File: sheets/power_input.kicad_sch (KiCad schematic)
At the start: 106 parts, among them J2 TYPE-C-31-M-12, Q20 FDMS86250, Q21 FDMC2523P, Q22 BSC057N08NS3 G, Q23 BSC057N08NS3 G, Q24 FCX493TA, Q25 FCX493TA, Q30 IRLR7843TRPBF, Q31 IRLR7843TRPBF, T1 750313355, U10 TPS23730RMTR, U19 LM5050MKX-1/NOPB, U2 CH224K, U20 TCMT1107, U21 LM5050MKX-1/NOPB, U22 TL431IDBVR, U23 FOD817DS

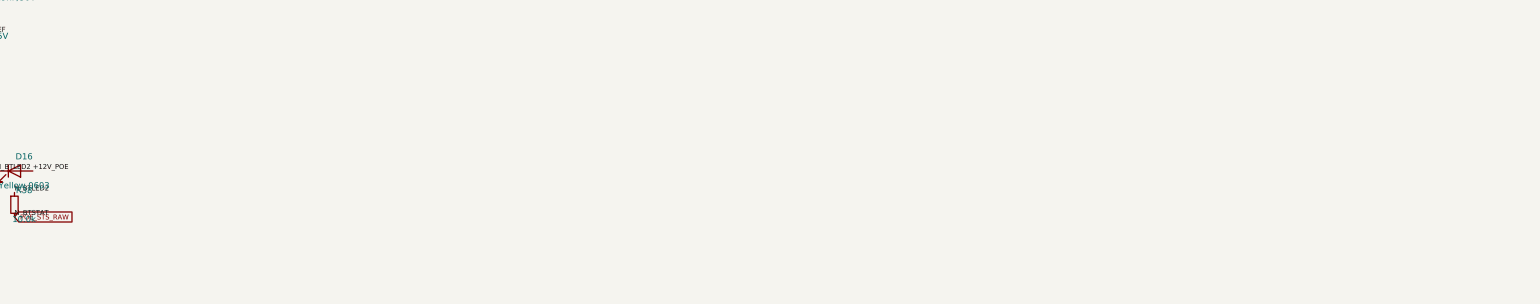
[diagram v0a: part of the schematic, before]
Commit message: sch: mcu fixes — XOUT crystal resistor, rail-to-rail LED kill, RGB series R, decoupling
Review pass on sheets/mcu.kicad_sch: swap R76 onto the XOUT side of Y1
(XIN direct, 1k limits drive into the crystal per the RPi RP2040 guide);
rebuild the LED-kill gate network rail-to-rail (Q35 2N7002 + repurposed
R82/R84 pull-ups replace the old resistive-mixing divider that left only
~0.2-0.3V of OFF-state Vgs margin — GP9/LED_EN_CTL is now active-low
kill); insert R92 (330R) between GP14 and U28 DIN with a net split
(RGB_DI/RGB_DIN); add decoupling (C78-C81 100nF at U25/U26/U27/RP2040's
9th supply pin, C82 1uF at VREG_VIN); add a Task-14 SW2 silk note and a
power_input.kicad_sch note on D16's unkillable ~75uA glow.

uv run tools/check_nets.py: all pass (new + all pre-existing lines).
kicad-cli sch erc: 0 errors / 611 warnings (600 baseline +11, all
endpoint_off_grid, no new category — see docs/erc-waivers.md).
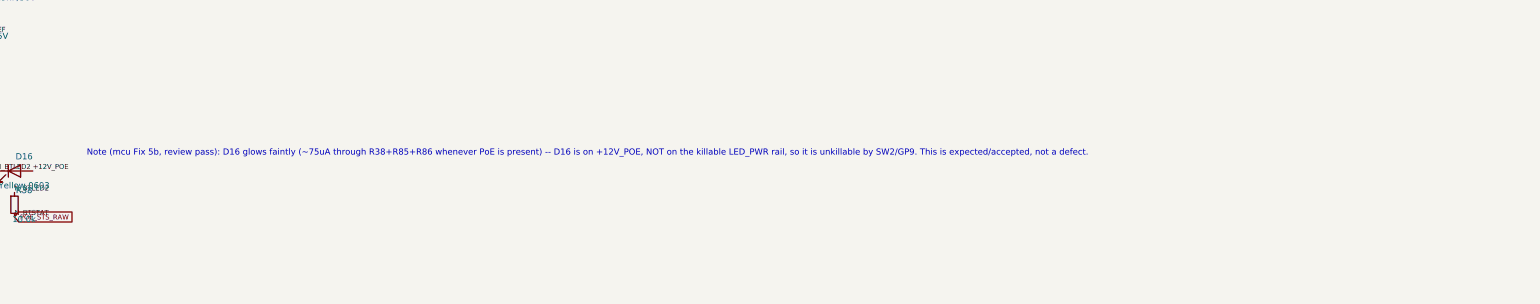
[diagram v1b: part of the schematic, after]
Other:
- note added: "Note (mcu Fix 5b, review pass): D16 glows faintly (~75uA through R38+R85+R86 whenever PoE is present) -- D16 is on +12V_POE, NOT on the killable LED_PWR rail, so it is unkillable by SW2/GP9. This is expected/accepted, not a defect."
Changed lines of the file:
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@@
 		)
+	)
+	(text "Note (mcu Fix 5b, review pass): D16 glows faintly (~75uA through R38+R85+R86 whenever PoE is present) -- D16 is on +12V_POE, NOT on the killable LED_PWR rail, so it is unkillable by SW2/GP9. This is expected/accepted, not a defect."
+		(exclude_from_sim no)
+		(at 555 140 0)
+		(effects (font (size 1.27 1.27)) (justify left bottom))
 	)
 	(text "TODO(mcu): POE_STATUS net dropped on this sheet — EVM-093 exposes BT only as an isolated LED indicator (U23 opto, D16/R38 from +12V_POE). Node N_BTSTAT swings ~0-11V, NOT 3V3-safe. Re-plan the MCU status input (e.g. repurpose U23 collector with a +3V3 pull-up in place of the D16/R38 LED chain) before wiring the mcu sheet."
